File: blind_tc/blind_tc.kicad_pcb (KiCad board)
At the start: 2 copper layers, 106 x 50 mm, 4 parts

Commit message: exported gerbers
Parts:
- added G***: LOGO, otter:usb-temperature-logger-otter, F.Cu at (89.3, 69.6)
- added G***: LOGO, otter:usb-temperature-logger-text, F.Cu at (103.0, 74.0)
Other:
- outline, holes or cut-outs redrawn

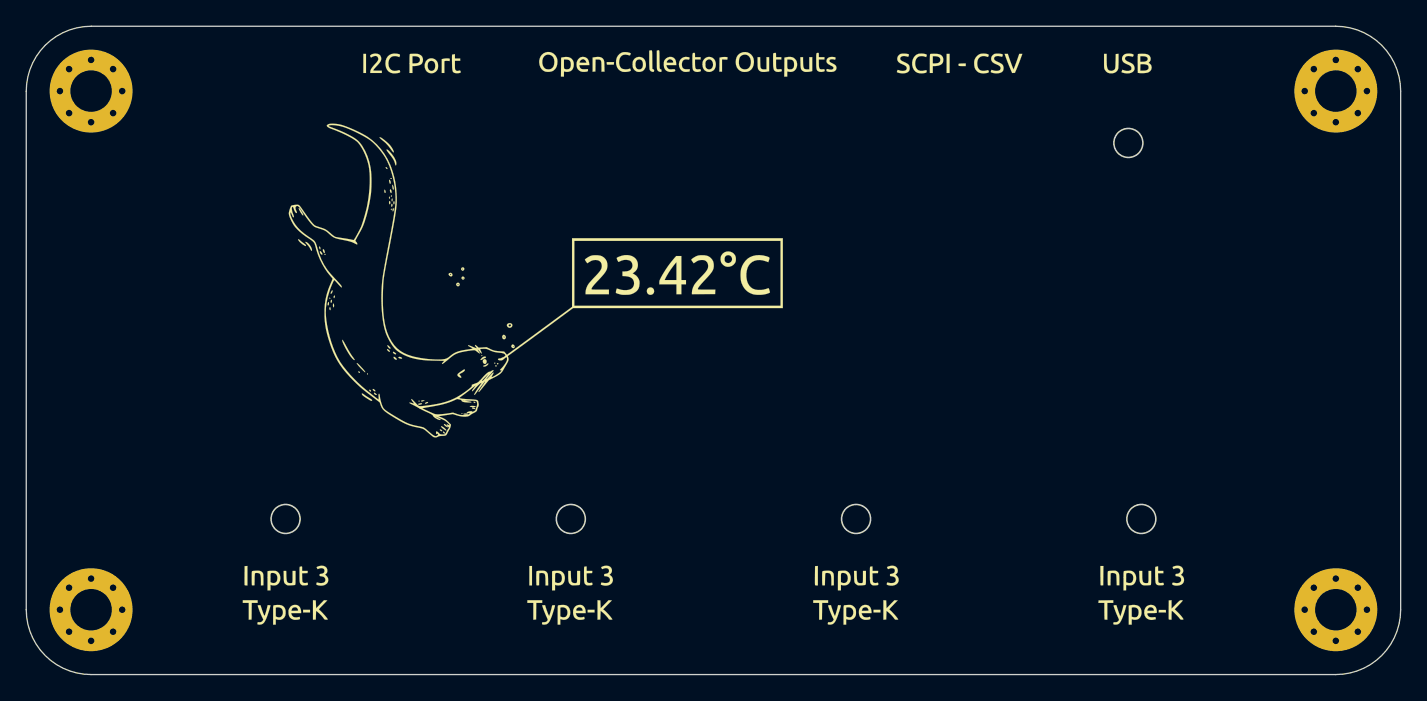
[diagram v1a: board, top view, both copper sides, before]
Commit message: updated blind to kicad 6
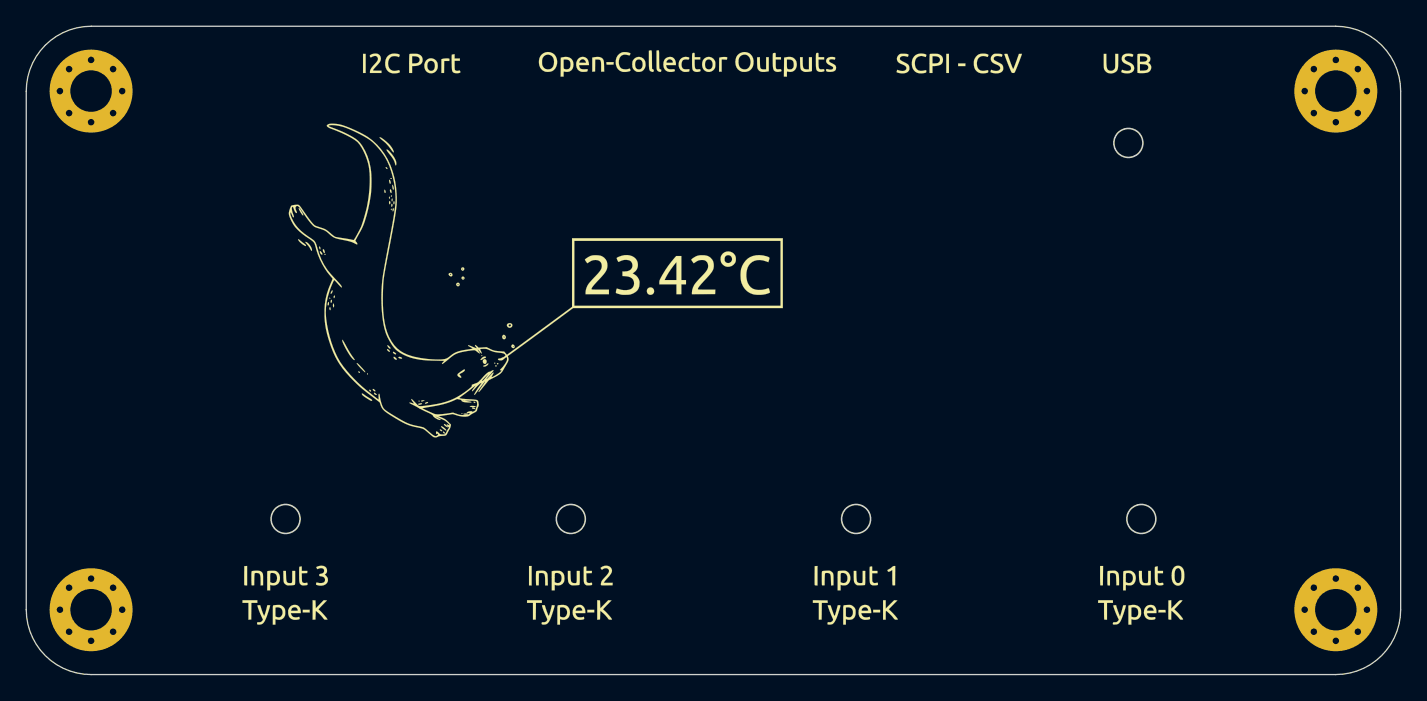
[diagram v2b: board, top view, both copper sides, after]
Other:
- net class Default removed
